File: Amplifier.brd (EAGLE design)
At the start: 60.3 x 55.2 mm, 34 parts, among them IC1 OP213, J1 ARDUINO_R3_SHIELD

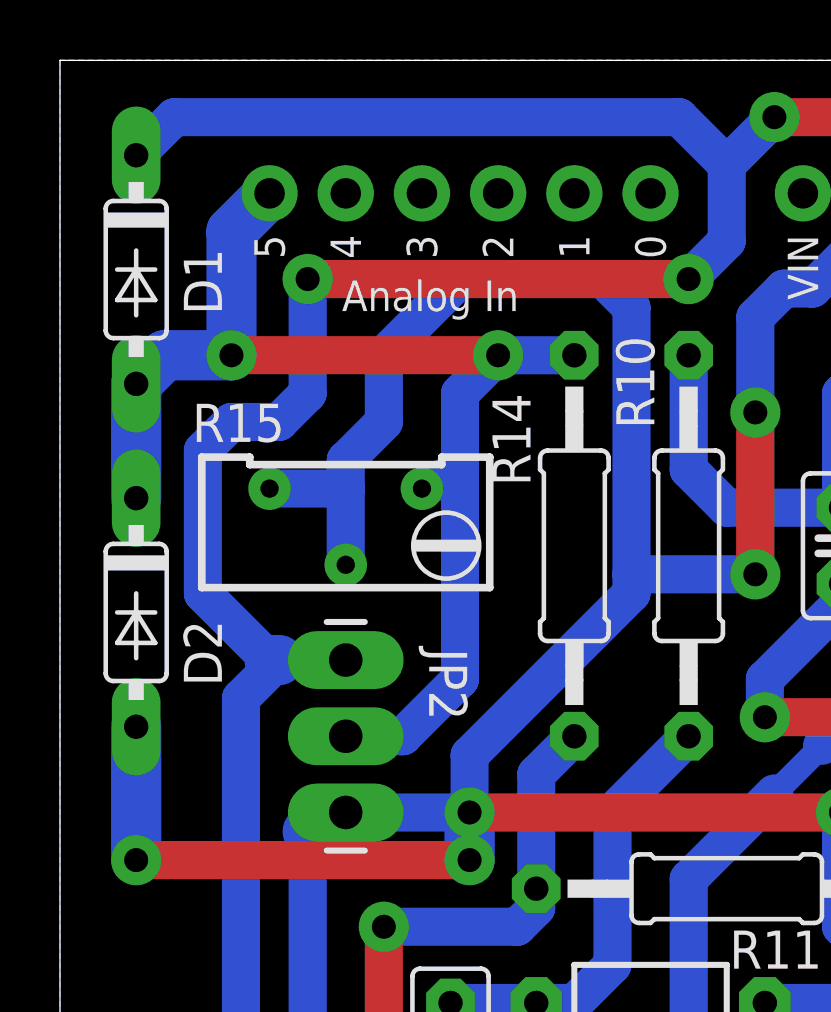
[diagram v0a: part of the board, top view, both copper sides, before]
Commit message: Stupid bug in output stage fixed
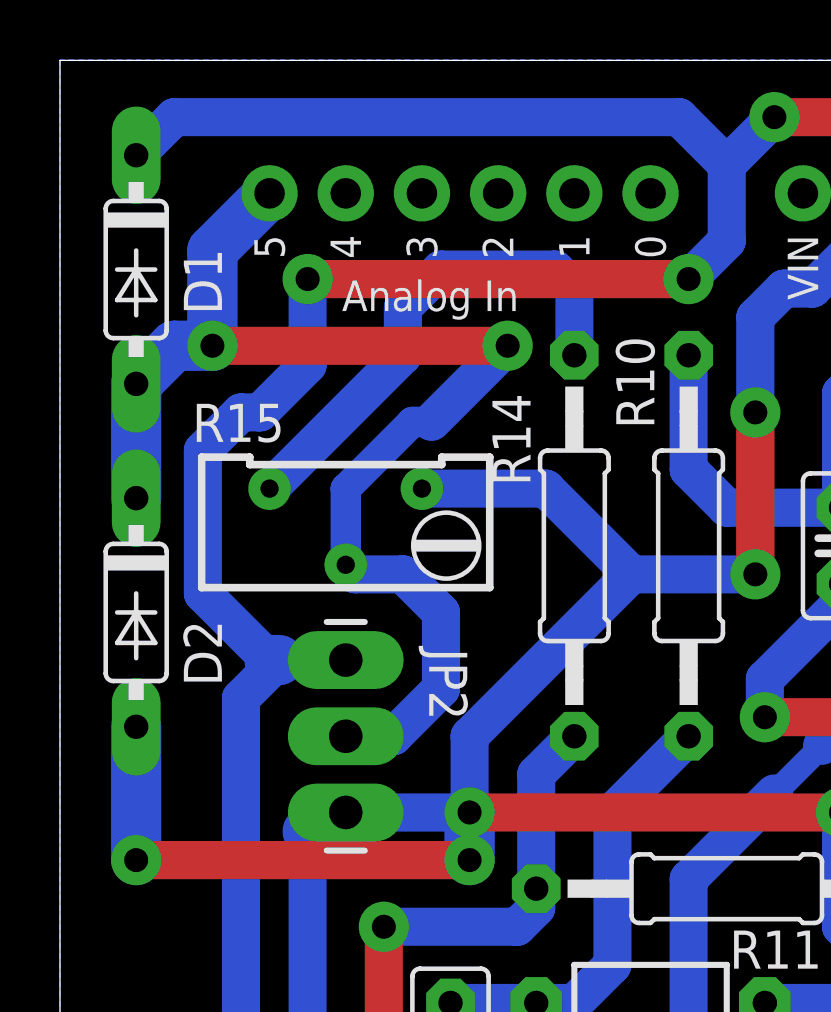
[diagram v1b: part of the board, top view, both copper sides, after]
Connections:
- new net N$18: R14.1, R15.3
- net GEOPHONE_OUT: now also R15.2; no longer R14.1, R15.1
- net GND: now also R15.1; no longer R15.2, R15.3
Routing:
- net GND: track 187.3 -> 166.8 mm
- net N$18: track 0.00 -> 16.6 mm
- net GEOPHONE_OUT: track 42.1 -> 42.7 mm
- net VCC: track 167.4 -> 166.8 mm
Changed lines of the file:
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@@
 <wire x1="6.985" y1="35.2425" x2="4.7625" y2="37.465" width="1.27" layer="16"/>
 <wire x1="4.7625" y1="37.465" x2="4.7625" y2="42.2275" width="1.27" layer="16"/>
-<wire x1="4.7625" y1="42.2275" x2="5.715" y2="43.18" width="1.27" layer="16"/>
-<wire x1="5.715" y1="43.18" x2="7.3025" y2="43.18" width="1.27" layer="16"/>
-<wire x1="7.3025" y1="43.18" x2="8.255" y2="44.1325" width="1.27" layer="16"/>
-<wire x1="8.255" y1="44.1325" x2="8.255" y2="47.9425" width="1.27" layer="16"/>
+<wire x1="4.7625" y1="42.2275" x2="6.0325" y2="43.4975" width="1.27" layer="16"/>
+<wire x1="6.0325" y1="43.4975" x2="6.6675" y2="43.4975" width="1.27" layer="16"/>
+<wire x1="6.6675" y1="43.4975" x2="8.255" y2="45.085" width="1.27" layer="16"/>
+<wire x1="8.255" y1="45.085" x2="8.255" y2="47.9425" width="1.27" layer="16"/>
 <via x="8.255" y="47.9425" extent="1-16" drill="0.8" diameter="1.6764" shape="square"/>
 <wire x1="9.525" y1="35.2425" x2="7.3025" y2="35.2425" width="1.27" layer="16"/>
@@
 <wire x1="45.085" y1="26.3525" x2="45.085" y2="28.8925" width="1.27" layer="16"/>
 <wire x1="9.525" y1="30.1625" x2="13.6525" y2="30.1625" width="1.27" layer="16"/>
-<contactref element="R15" pad="3"/>
-<contactref element="R15" pad="2"/>
-<wire x1="6.985" y1="40.9575" x2="9.525" y2="40.9575" width="1.27" layer="16"/>
-<wire x1="9.525" y1="40.9575" x2="9.525" y2="41.91" width="1.27" layer="16"/>
-<wire x1="9.525" y1="41.91" x2="10.795" y2="43.18" width="1.27" layer="16"/>
-<wire x1="10.795" y1="43.18" x2="10.795" y2="45.4025" width="1.27" layer="16"/>
-<wire x1="10.795" y1="45.4025" x2="13.335" y2="47.9425" width="1.27" layer="16"/>
-<wire x1="13.335" y1="47.9425" x2="18.0975" y2="47.9425" width="1.27" layer="16"/>
-<wire x1="18.0975" y1="47.9425" x2="19.05" y2="46.99" width="1.27" layer="16"/>
-<wire x1="13.6525" y1="32.0675" x2="13.6525" y2="30.1625" width="1.27" layer="16"/>
-<wire x1="9.525" y1="38.4175" x2="9.525" y2="40.9575" width="1.27" layer="16"/>
-<wire x1="13.6525" y1="32.0675" x2="19.05" y2="37.465" width="1.27" layer="16"/>
-<wire x1="19.05" y1="37.465" x2="19.05" y2="38.1" width="1.27" layer="16"/>
-<wire x1="19.05" y1="38.1" x2="19.05" y2="46.99" width="1.27" layer="16"/>
+<wire x1="13.6525" y1="32.7025" x2="13.6525" y2="30.1625" width="1.27" layer="16"/>
+<wire x1="13.6525" y1="32.7025" x2="19.05" y2="38.1" width="1.27" layer="16"/>
 <contactref element="IC1" pad="4"/>
 <contactref element="J1" pad="GND@2"/>
@@
 <wire x1="27.94" y1="20.955" x2="27.94" y2="22.5425" width="1.27" layer="16"/>
 <wire x1="27.94" y1="22.5425" x2="26.67" y2="23.8125" width="1.27" layer="16"/>
+<contactref element="R15" pad="1"/>
+<wire x1="12.065" y1="40.9575" x2="16.1925" y2="40.9575" width="1.27" layer="16"/>
+<wire x1="16.1925" y1="40.9575" x2="19.05" y2="38.1" width="1.27" layer="16"/>
 </signal>
 <signal name="GEOPHONE_OUT">
-<contactref element="R14" pad="1"/>
 <contactref element="JP2" pad="2"/>
-<wire x1="9.525" y1="32.7025" x2="11.43" y2="32.7025" width="1.27" layer="16"/>
-<wire x1="11.43" y1="32.7025" x2="13.335" y2="34.6075" width="1.27" layer="16"/>
-<wire x1="13.335" y1="34.6075" x2="13.335" y2="41.5925" width="1.27" layer="16"/>
-<contactref element="R15" pad="1"/>
-<wire x1="12.065" y1="40.9575" x2="13.335" y2="41.5925" width="1.27" layer="16"/>
 <contactref element="J1" pad="A5"/>
-<wire x1="13.335" y1="41.5925" x2="13.335" y2="44.1325" width="1.27" layer="16"/>
-<wire x1="13.335" y1="44.1325" x2="14.605" y2="45.4025" width="1.27" layer="16"/>
-<via x="14.605" y="45.4025" extent="1-16" drill="0.8" diameter="1.6764" shape="square"/>
-<wire x1="14.605" y1="45.4025" x2="5.715" y2="45.4025" width="1.27" layer="1"/>
-<via x="5.715" y="45.4025" extent="1-16" drill="0.8" diameter="1.6764" shape="square"/>
-<wire x1="5.715" y1="45.4025" x2="5.715" y2="49.53" width="1.6764" layer="16"/>
-<wire x1="5.715" y1="49.53" x2="6.985" y2="50.8" width="1.6764" layer="16"/>
-<wire x1="14.605" y1="45.4025" x2="17.145" y2="45.4025" width="1.27" layer="16"/>
+<wire x1="12.3825" y1="43.18" x2="14.9225" y2="45.72" width="1.27" layer="16"/>
+<via x="14.9225" y="45.72" extent="1-16" drill="0.8" diameter="1.6764" shape="square"/>
+<wire x1="14.9225" y1="45.72" x2="5.08" y2="45.72" width="1.27" layer="1"/>
+<via x="5.08" y="45.72" extent="1-16" drill="0.8" diameter="1.6764" shape="square"/>
+<wire x1="5.08" y1="45.72" x2="5.08" y2="48.895" width="1.6764" layer="16"/>
+<wire x1="5.08" y1="48.895" x2="6.985" y2="50.8" width="1.6764" layer="16"/>
 <contactref element="D1" pad="A"/>
 <contactref element="D2" pad="C"/>
-<wire x1="5.715" y1="45.4025" x2="3.4925" y2="45.4025" width="1.6764" layer="16"/>
-<wire x1="3.4925" y1="45.4025" x2="2.54" y2="44.45" width="1.6764" layer="16"/>
+<wire x1="5.08" y1="45.72" x2="3.81" y2="45.72" width="1.6764" layer="16"/>
+<wire x1="3.81" y1="45.72" x2="2.54" y2="44.45" width="1.6764" layer="16"/>
 <wire x1="2.54" y1="44.45" x2="2.54" y2="40.64" width="1.6764" layer="16"/>
+<contactref element="R15" pad="2"/>
+<wire x1="9.525" y1="38.4175" x2="9.525" y2="40.9575" width="1.016" layer="16"/>
+<wire x1="9.525" y1="40.9575" x2="11.7475" y2="43.18" width="1.016" layer="16"/>
+<wire x1="11.7475" y1="43.18" x2="12.3825" y2="43.18" width="1.016" layer="16"/>
+<wire x1="9.525" y1="32.7025" x2="11.1125" y2="32.7025" width="1.27" layer="16"/>
+<wire x1="11.1125" y1="32.7025" x2="12.7" y2="34.29" width="1.27" layer="16"/>
+<wire x1="12.7" y1="34.29" x2="12.7" y2="36.83" width="1.27" layer="16"/>
+<wire x1="12.7" y1="36.83" x2="11.43" y2="38.1" width="1.27" layer="16"/>
+<wire x1="11.43" y1="38.1" x2="9.8425" y2="38.1" width="1.27" layer="16"/>
+<wire x1="9.8425" y1="38.1" x2="9.525" y2="38.4175" width="1.27" layer="16"/>
 </signal>
 <signal name="N$14">
@@
 <wire x1="50.4825" y1="46.99" x2="56.515" y2="46.99" width="1.4224" layer="16"/>
 </signal>
+<signal name="N$18">
+<contactref element="R14" pad="1"/>
+<contactref element="R15" pad="3"/>
+<wire x1="17.145" y1="45.4025" x2="17.145" y2="47.625" width="1.27" layer="16"/>
+<wire x1="17.145" y1="47.625" x2="16.51" y2="48.26" width="1.27" layer="16"/>
+<wire x1="16.51" y1="48.26" x2="12.7" y2="48.26" width="1.27" layer="16"/>
+<wire x1="12.7" y1="48.26" x2="11.43" y2="46.99" width="1.27" layer="16"/>
+<wire x1="11.43" y1="46.99" x2="11.43" y2="45.4025" width="1.27" layer="16"/>
+<wire x1="11.43" y1="45.4025" x2="6.985" y2="40.9575" width="1.27" layer="16"/>
+</signal>
 </signals>
